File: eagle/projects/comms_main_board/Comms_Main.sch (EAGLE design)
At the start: 132 parts, among them J10 MOL-KK-2-RA, J11 MOL-KK-3P-RA, J12 MOL-KK-3P-RA, J13 MOL-KK-3P-RA, J14 MOL-KK-3P-RA, J15 MOL-KK-2-RA, J16 MOLKK_POW_2_RA, J17 MOLKK_POW_2_RA, J18 MOLKK_POW_2_RA, J19 MOLKK_POW_2_RA, J2 PRT-12639, J20 MOL-KK-2-RA, J3 PRT-12639, J4 PRT-12639, J5 PRT-12639, J6 MOL-KK-3P-RA, J7 MOL-KK-5P-V, J8 RECEPTACLE-2x20-254MM, J9 MOL-KK-3P-RA, Q1 CSD17579Q3A, U1 TPS562209DDCT, U11 TPS562209DDCT, U14 MAX4311, U2 LP2985-33DBVR, U3 LP5900TLX-3.3/NOPB, U4 TPS562209DDCT, U5 LMZ34002RKGR, U6 LM3488MMX/NOPB, U7 PCT2075D,118, U8 MS560702BA03-50, U9 MAX-M8Q

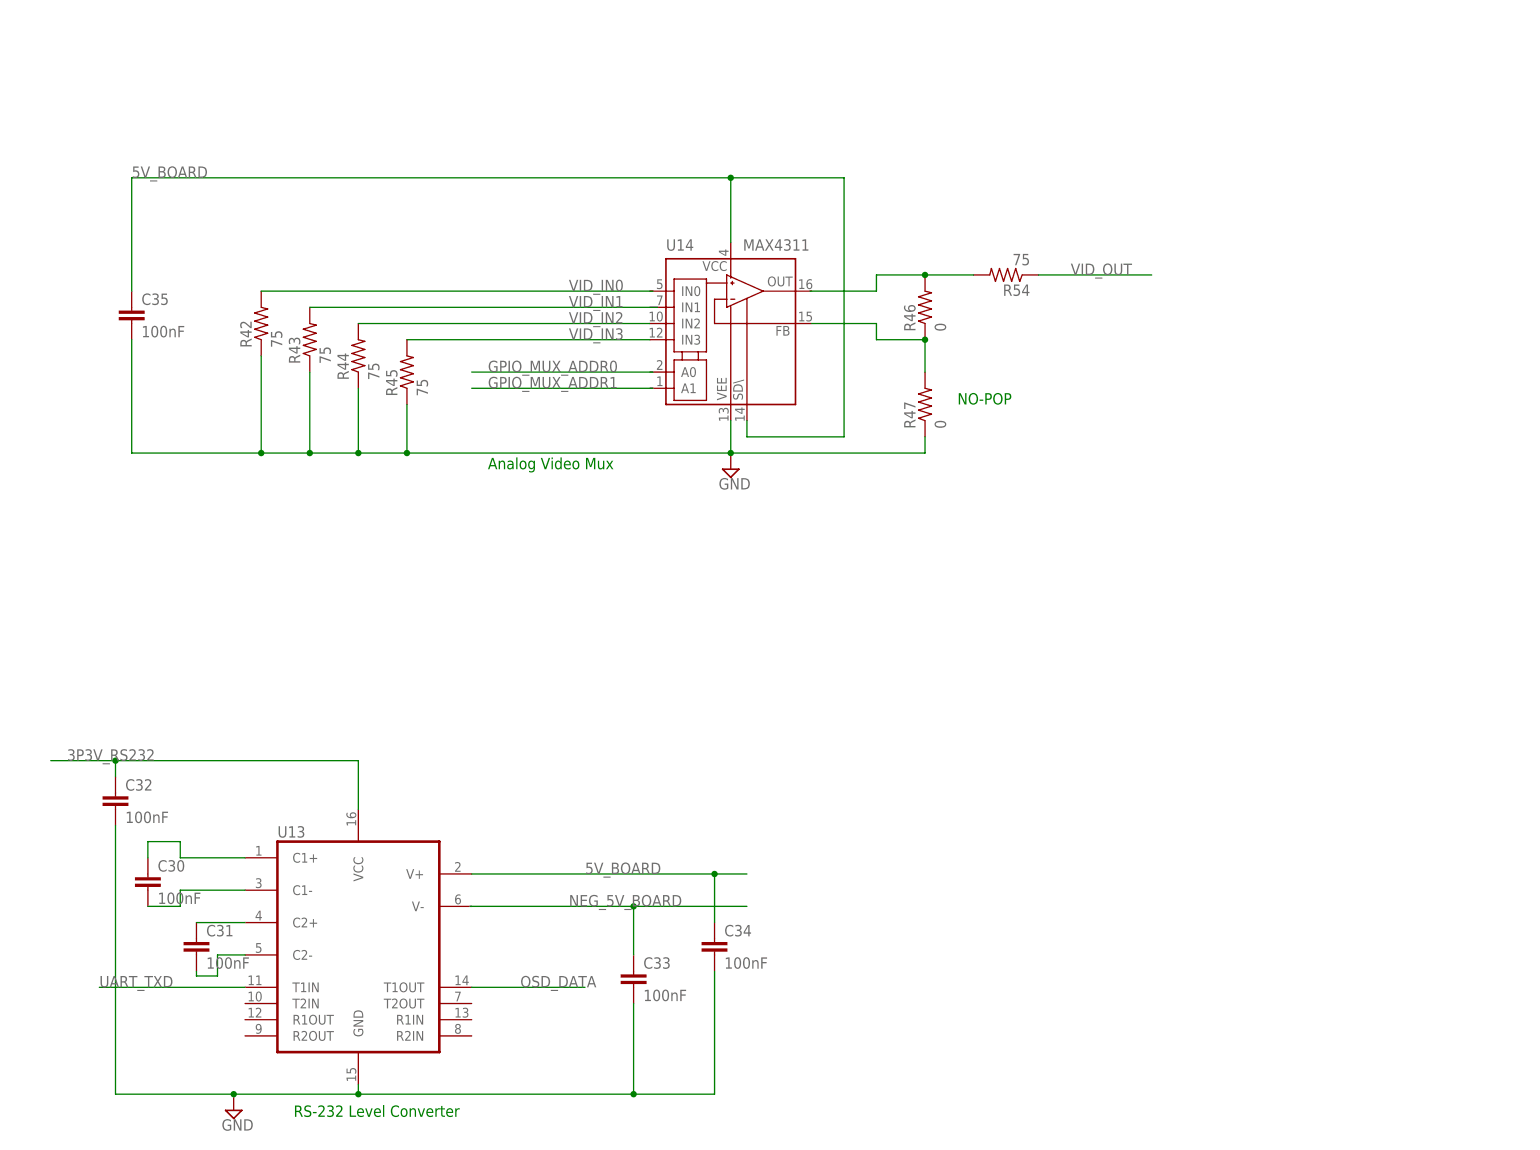
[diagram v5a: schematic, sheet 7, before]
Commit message: Finished connectors for comms schematic
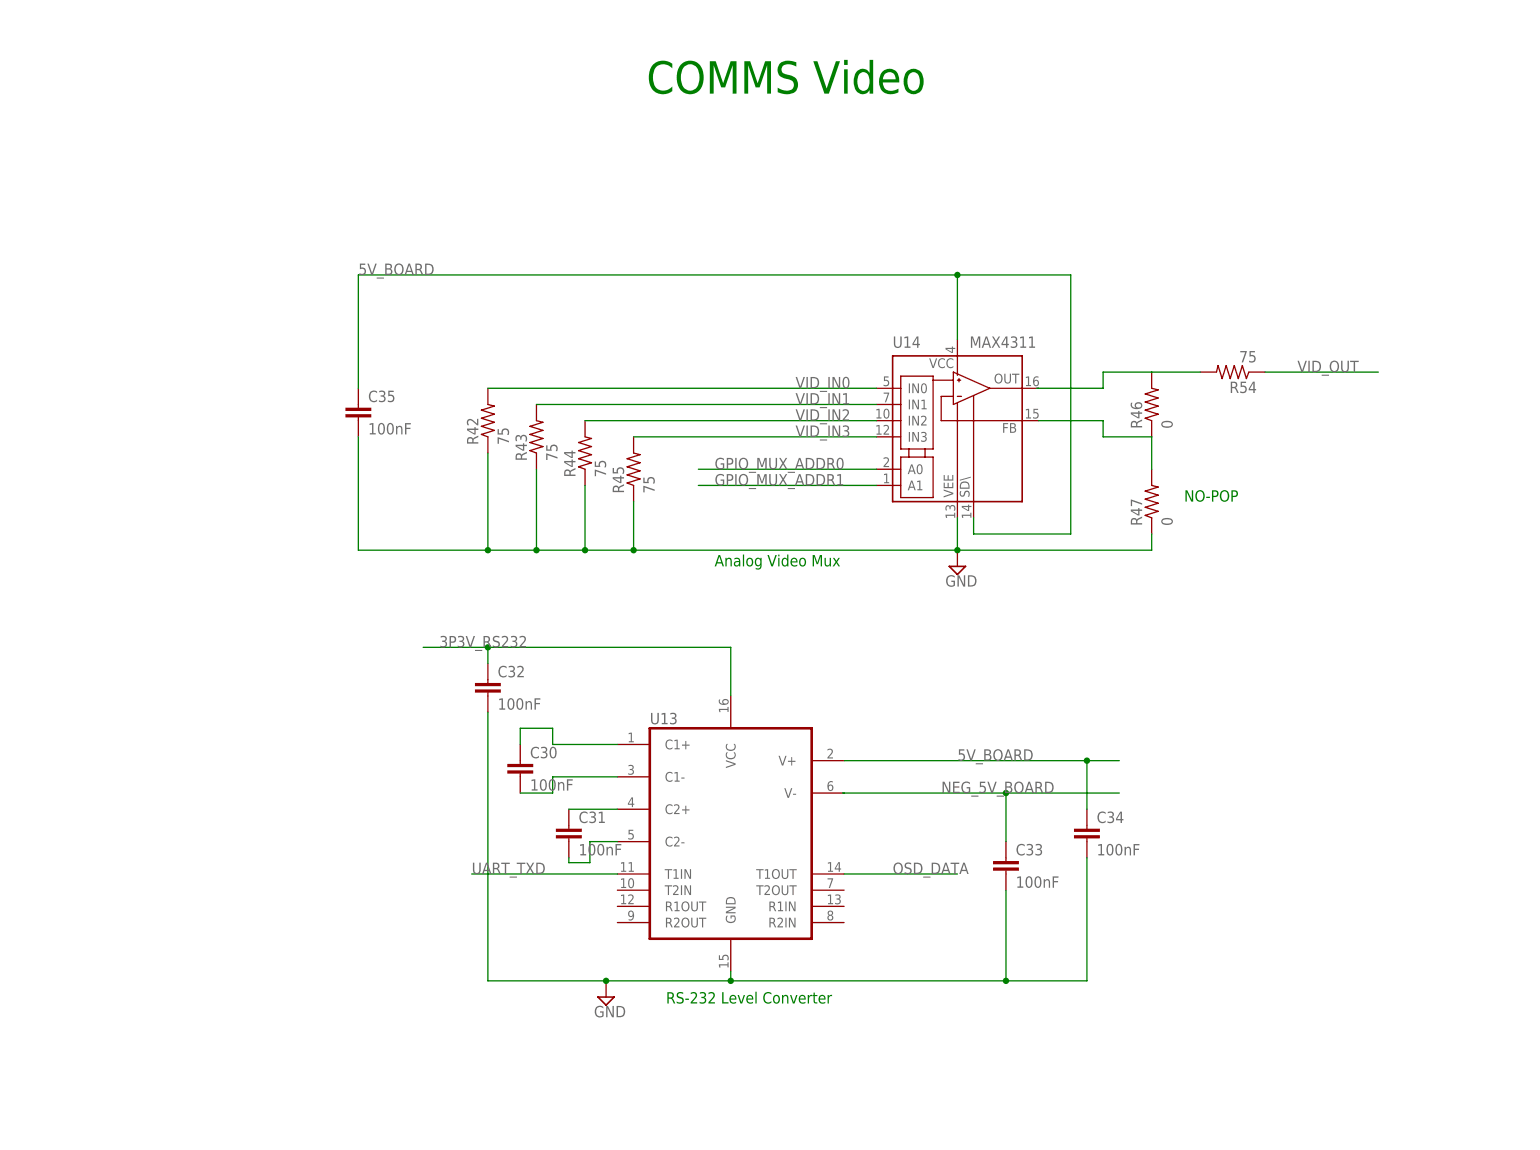
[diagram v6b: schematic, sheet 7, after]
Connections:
- new net GPIO_MUX_ADDR0: U14.A0
- new net GPIO_MUX_ADDR1: U14.A1
- net N$58: now also U14.OUT
- net VID_IN0: now also U14.IN0
- net VID_IN1: now also U14.IN1
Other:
- note added: "COMMS Video"
- moved on the sheet: C30, C31, C32, C33, C34, C35, R42, R43, R44, R45, R46, R47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

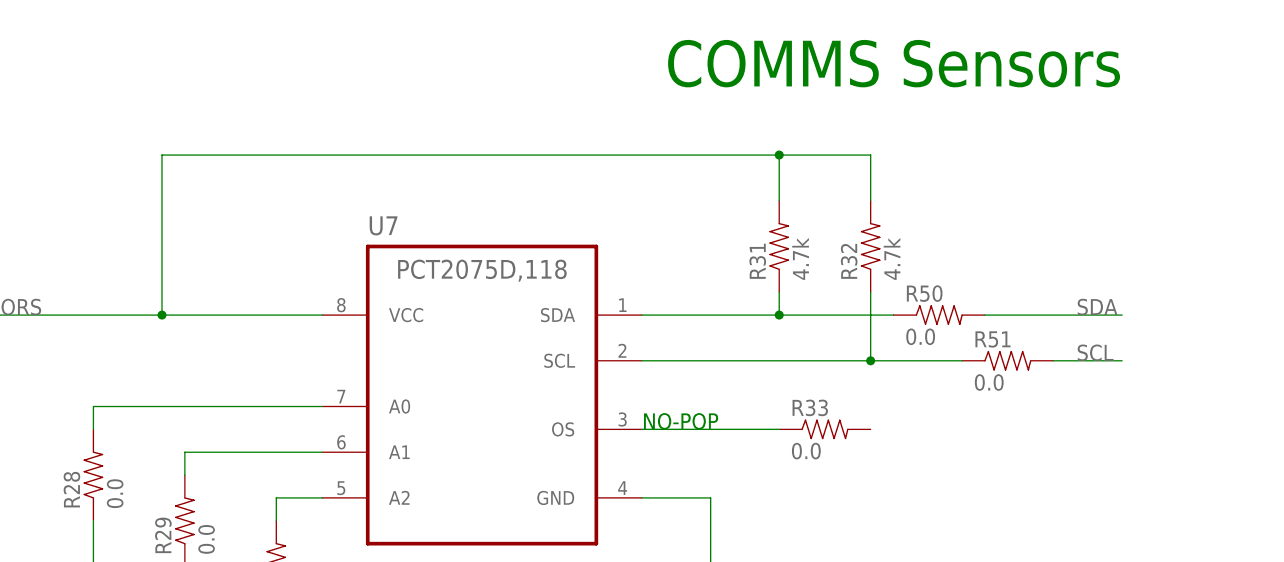
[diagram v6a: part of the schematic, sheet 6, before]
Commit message: Swapped i2c pull up resistor location
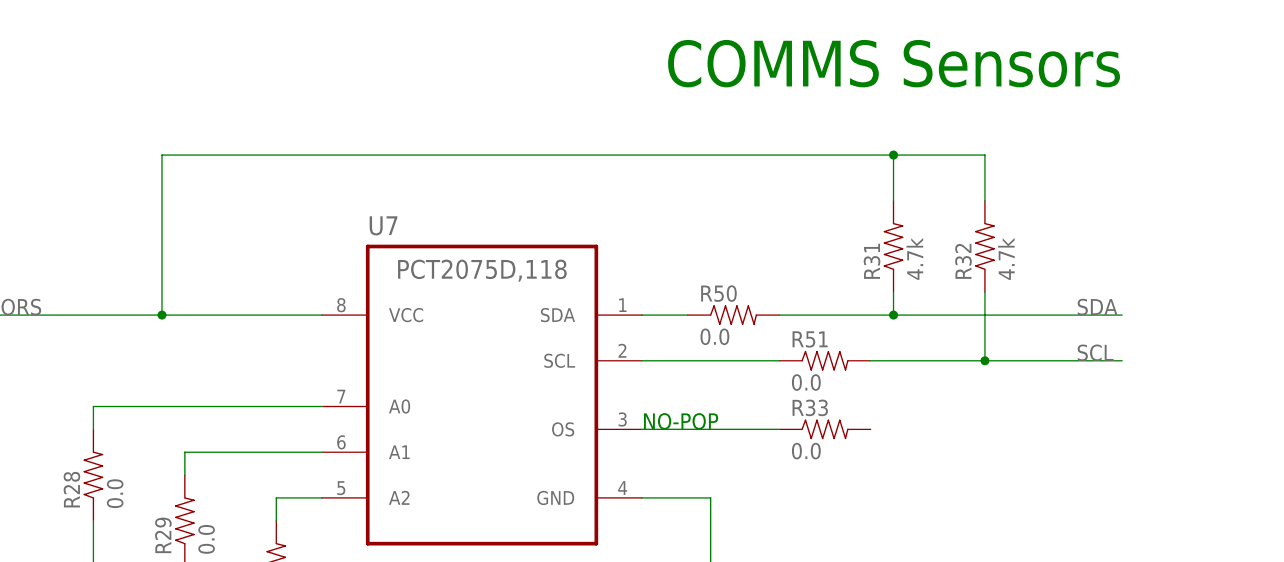
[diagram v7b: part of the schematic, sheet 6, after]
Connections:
- net SCL: now also R32.1
- net SDA: now also R31.1
- net TEMP_SCL: no longer R32.1
- net TEMP_SDA: no longer R31.1
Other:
- moved on the sheet: R31, R32, R50, R51
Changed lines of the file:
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@@
 <instance part="R30" gate="G$1" x="58.42" y="114.3" rot="R90"/>
 <instance part="SUPPLY9" gate="GND" x="48.26" y="99.06"/>
-<instance part="R31" gate="G$1" x="114.3" y="149.86" rot="R90"/>
-<instance part="R32" gate="G$1" x="124.46" y="149.86" rot="R90"/>
+<instance part="R31" gate="G$1" x="127" y="149.86" rot="R90"/>
+<instance part="R32" gate="G$1" x="137.16" y="149.86" rot="R90"/>
 <instance part="R33" gate="G$1" x="119.38" y="129.54"/>
 <instance part="U8" gate="G$1" x="81.28" y="38.1"/>
@@
 <instance part="R48" gate="G$1" x="116.84" y="45.72"/>
 <instance part="R49" gate="G$1" x="127" y="40.64"/>
-<instance part="R50" gate="G$1" x="132.08" y="142.24"/>
-<instance part="R51" gate="G$1" x="139.7" y="137.16"/>
+<instance part="R50" gate="G$1" x="109.22" y="142.24"/>
+<instance part="R51" gate="G$1" x="119.38" y="137.16"/>
 <instance part="R52" gate="G$1" x="137.16" y="86.36"/>
 <instance part="R53" gate="G$1" x="137.16" y="76.2"/>
@@
 <wire x1="45.72" y1="142.24" x2="17.78" y2="142.24" width="0.1524" layer="91"/>
 <wire x1="17.78" y1="142.24" x2="7.62" y2="142.24" width="0.1524" layer="91"/>
-<wire x1="114.3" y1="154.94" x2="114.3" y2="160.02" width="0.1524" layer="91"/>
-<wire x1="114.3" y1="160.02" x2="45.72" y2="160.02" width="0.1524" layer="91"/>
+<wire x1="127" y1="154.94" x2="127" y2="160.02" width="0.1524" layer="91"/>
+<wire x1="127" y1="160.02" x2="45.72" y2="160.02" width="0.1524" layer="91"/>
 <wire x1="45.72" y1="160.02" x2="45.72" y2="142.24" width="0.1524" layer="91"/>
 <junction x="45.72" y="142.24"/>
 <pinref part="R32" gate="G$1" pin="2"/>
-<wire x1="124.46" y1="154.94" x2="124.46" y2="160.02" width="0.1524" layer="91"/>
-<wire x1="124.46" y1="160.02" x2="114.3" y2="160.02" width="0.1524" layer="91"/>
-<junction x="114.3" y="160.02"/>
+<wire x1="137.16" y1="154.94" x2="137.16" y2="160.02" width="0.1524" layer="91"/>
+<wire x1="137.16" y1="160.02" x2="127" y2="160.02" width="0.1524" layer="91"/>
+<junction x="127" y="160.02"/>
 <pinref part="C23" gate="G$1" pin="2"/>
 <wire x1="17.78" y1="139.7" x2="17.78" y2="142.24" width="0.1524" layer="91"/>
@@
 </segment>
 <segment>
-<wire x1="137.16" y1="142.24" x2="152.4" y2="142.24" width="0.1524" layer="91"/>
+<wire x1="114.3" y1="142.24" x2="127" y2="142.24" width="0.1524" layer="91"/>
 <pinref part="R50" gate="G$1" pin="2"/>
 <label x="147.32" y="142.24" size="1.778" layer="95"/>
+<pinref part="R31" gate="G$1" pin="1"/>
+<wire x1="127" y1="142.24" x2="152.4" y2="142.24" width="0.1524" layer="91"/>
+<wire x1="127" y1="144.78" x2="127" y2="142.24" width="0.1524" layer="91"/>
+<junction x="127" y="142.24"/>
 </segment>
 <segment>
@@
 </segment>
 <segment>
-<wire x1="144.78" y1="137.16" x2="152.4" y2="137.16" width="0.1524" layer="91"/>
+<wire x1="124.46" y1="137.16" x2="137.16" y2="137.16" width="0.1524" layer="91"/>
 <pinref part="R51" gate="G$1" pin="2"/>
 <label x="147.32" y="137.16" size="1.778" layer="95"/>
+<pinref part="R32" gate="G$1" pin="1"/>
+<wire x1="137.16" y1="137.16" x2="152.4" y2="137.16" width="0.1524" layer="91"/>
+<wire x1="137.16" y1="144.78" x2="137.16" y2="137.16" width="0.1524" layer="91"/>
+<junction x="137.16" y="137.16"/>
 </segment>
 <segment>
@@
 <segment>
 <pinref part="U7" gate="A" pin="SDA"/>
-<wire x1="99.06" y1="142.24" x2="114.3" y2="142.24" width="0.1524" layer="91"/>
-<pinref part="R31" gate="G$1" pin="1"/>
-<wire x1="114.3" y1="142.24" x2="127" y2="142.24" width="0.1524" layer="91"/>
-<wire x1="114.3" y1="144.78" x2="114.3" y2="142.24" width="0.1524" layer="91"/>
-<junction x="114.3" y="142.24"/>
+<wire x1="99.06" y1="142.24" x2="104.14" y2="142.24" width="0.1524" layer="91"/>
 <pinref part="R50" gate="G$1" pin="1"/>
 </segment>
@@
 <segment>
 <pinref part="U7" gate="A" pin="SCL"/>
-<wire x1="99.06" y1="137.16" x2="124.46" y2="137.16" width="0.1524" layer="91"/>
-<pinref part="R32" gate="G$1" pin="1"/>
-<wire x1="124.46" y1="137.16" x2="134.62" y2="137.16" width="0.1524" layer="91"/>
-<wire x1="124.46" y1="144.78" x2="124.46" y2="137.16" width="0.1524" layer="91"/>
-<junction x="124.46" y="137.16"/>
+<wire x1="99.06" y1="137.16" x2="114.3" y2="137.16" width="0.1524" layer="91"/>
 <pinref part="R51" gate="G$1" pin="1"/>
 </segment>
